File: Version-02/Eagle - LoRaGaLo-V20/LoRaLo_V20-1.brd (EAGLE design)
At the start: 69.5 x 82.5 mm, 31 parts, among them U2 RFM95WSMD

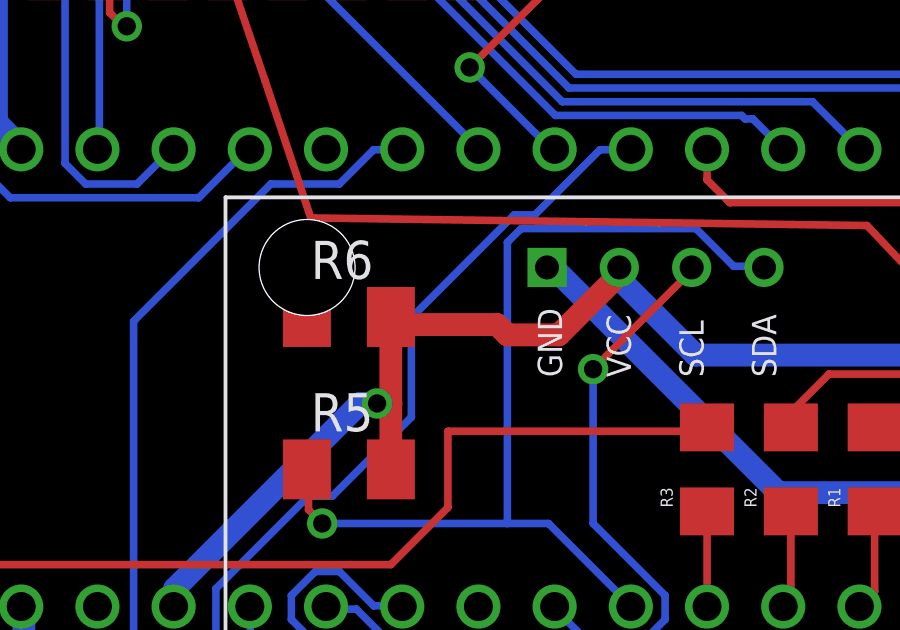
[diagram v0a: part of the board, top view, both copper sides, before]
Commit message: one trace fixed
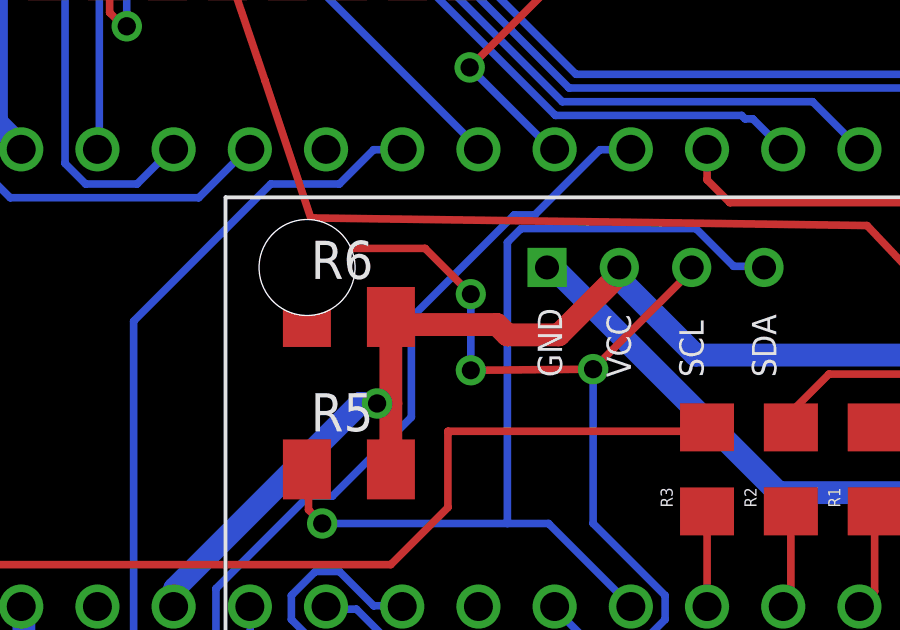
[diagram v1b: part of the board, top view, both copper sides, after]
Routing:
- net SCL0: track 18.6 -> 33.0 mm, vias 1 -> 3
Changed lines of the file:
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@@
 <wire x1="22.6314" y1="38.5191" x2="22.606" y2="38.608" width="0.254" layer="16"/>
 <via x="23.8887" y="46.5201" extent="1-16" drill="0.6096"/>
-<wire x1="23.8887" y1="46.5201" x2="14.348" y2="48.26" width="0" layer="19" extent="1-1"/>
+<wire x1="23.8887" y1="46.5201" x2="19.812" y2="46.482" width="0.254" layer="1"/>
+<via x="19.812" y="46.482" extent="1-16" drill="0.6"/>
+<wire x1="19.812" y1="46.482" x2="19.812" y2="49.022" width="0.254" layer="16"/>
+<via x="19.812" y="49.022" extent="1-16" drill="0.6"/>
+<wire x1="19.812" y1="49.022" x2="18.288" y2="50.546" width="0.254" layer="1"/>
+<wire x1="18.288" y1="50.546" x2="15.24" y2="50.546" width="0.254" layer="1"/>
+<wire x1="15.24" y1="50.546" x2="14.478" y2="49.784" width="0.254" layer="1"/>
+<wire x1="14.478" y1="49.784" x2="14.478" y2="48.39" width="0.254" layer="1"/>
+<wire x1="14.478" y1="48.39" x2="14.348" y2="48.26" width="0.254" layer="1"/>
 </signal>
 <signal name="DOWN">
